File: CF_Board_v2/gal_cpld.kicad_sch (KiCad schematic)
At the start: 18 parts, among them J2 JTAG, U10 74LVC1G07, U16 74LVC1G08, U7 GAL, U8 CPLD, U9 74LVC1G08, X2 40MHz

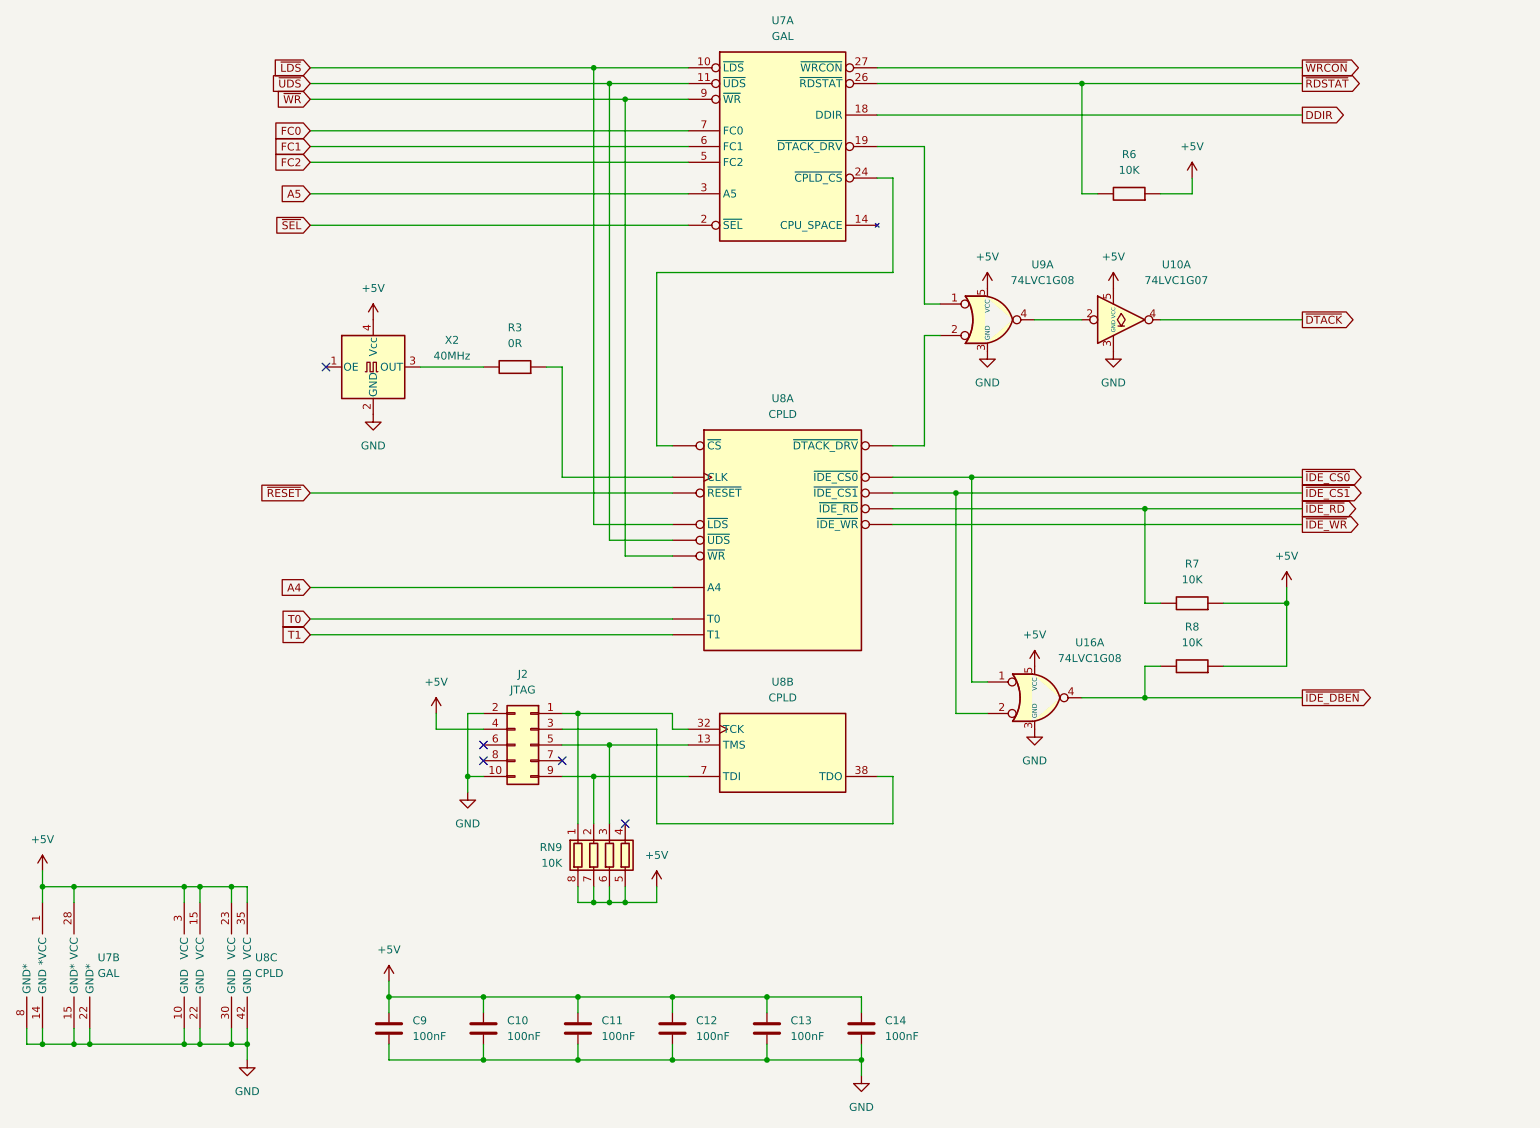
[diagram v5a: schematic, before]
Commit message: Modify control/status register to include CPLD timing select signals
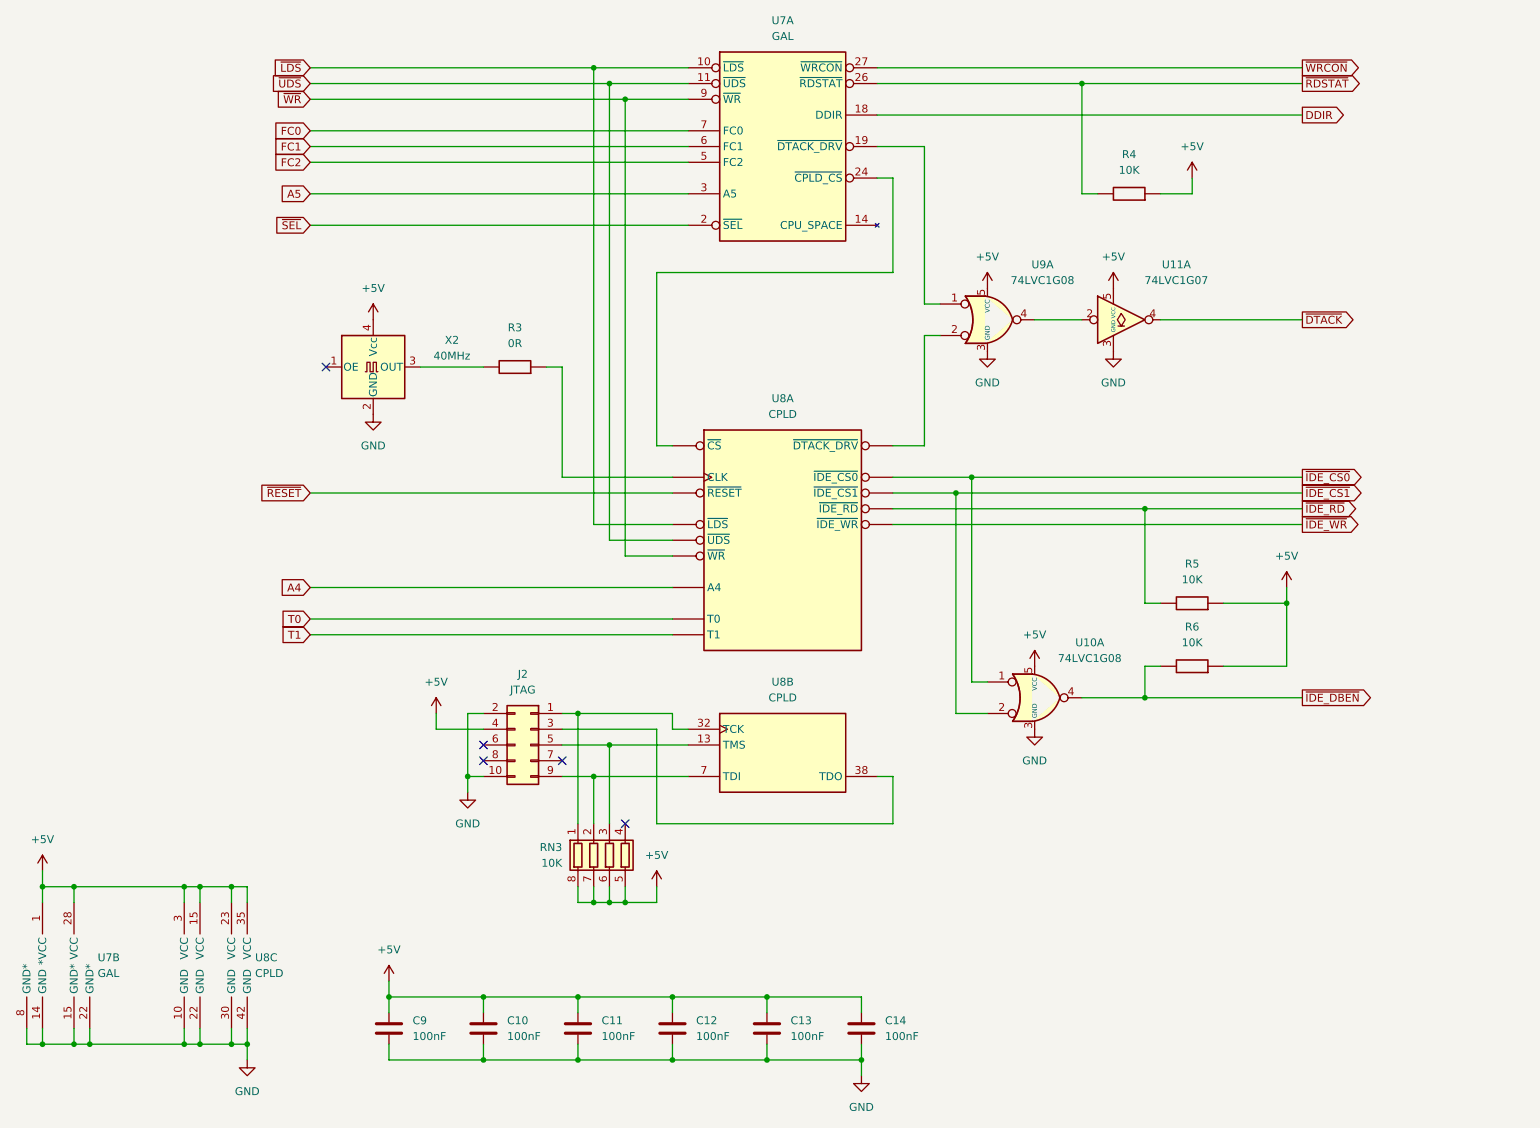
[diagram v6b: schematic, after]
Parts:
- renumbered R6 to R4, R7 to R5, R8 to R6, RN9 to RN3, U16 to U10, U10 to U11
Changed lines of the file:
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@@
   (symbol (lib_id "power:GND") (at 177.8 71.12 0) (unit 1)
     (in_bom yes) (on_board yes) (fields_autoplaced)
-    (property "Reference" "#PWR032" (id 0) (at 177.8 77.47 0)
+    (property "Reference" "#PWR035" (id 0) (at 177.8 77.47 0)
       (effects (font (size 1.27 1.27)) hide)
     )
@@
   (symbol (lib_id "power:+5V") (at 124.46 157.48 0) (unit 1)
     (in_bom yes) (on_board yes) (fields_autoplaced)
-    (property "Reference" "#PWR063" (id 0) (at 124.46 161.29 0)
+    (property "Reference" "#PWR032" (id 0) (at 124.46 161.29 0)
       (effects (font (size 1.27 1.27)) hide)
     )
@@
   (symbol (lib_id "COMET_symbols:74x1G08") (at 185.42 127 0) (unit 1) (convert 2)
     (in_bom yes) (on_board yes)
-    (property "Reference" "U16" (id 0) (at 194.31 118.11 0))
+    (property "Reference" "U10" (id 0) (at 194.31 118.11 0))
     (property "Value" "74LVC1G08" (id 1) (at 194.31 120.65 0))
     (property "Footprint" "COMET_footprints:Package_SOT23-5" (id 2) (at 185.42 127 0)
@@
   (symbol (lib_id "COMET_symbols:R") (at 200.66 45.72 90) (unit 1)
     (in_bom yes) (on_board yes) (fields_autoplaced)
-    (property "Reference" "R6" (id 0) (at 200.66 39.37 90))
+    (property "Reference" "R4" (id 0) (at 200.66 39.37 90))
     (property "Value" "10K" (id 1) (at 200.66 41.91 90))
     (property "Footprint" "COMET_footprints:R_SMD0805" (id 2) (at 200.66 45.72 0)
@@
   (symbol (lib_id "power:GND") (at 198.12 71.12 0) (unit 1)
     (in_bom yes) (on_board yes) (fields_autoplaced)
-    (property "Reference" "#PWR034" (id 0) (at 198.12 77.47 0)
+    (property "Reference" "#PWR039" (id 0) (at 198.12 77.47 0)
       (effects (font (size 1.27 1.27)) hide)
     )
@@
   (symbol (lib_id "power:+5V") (at 25.4 154.94 0) (unit 1)
     (in_bom yes) (on_board yes) (fields_autoplaced)
-    (property "Reference" "#PWR027" (id 0) (at 25.4 158.75 0)
+    (property "Reference" "#PWR025" (id 0) (at 25.4 158.75 0)
       (effects (font (size 1.27 1.27)) hide)
     )
@@
   (symbol (lib_id "power:+5V") (at 198.12 60.96 0) (unit 1)
     (in_bom yes) (on_board yes) (fields_autoplaced)
-    (property "Reference" "#PWR033" (id 0) (at 198.12 64.77 0)
+    (property "Reference" "#PWR038" (id 0) (at 198.12 64.77 0)
       (effects (font (size 1.27 1.27)) hide)
     )
@@
   (symbol (lib_id "COMET_symbols:74x1G08") (at 185.42 127 0) (unit 2)
     (in_bom yes) (on_board yes) (fields_autoplaced)
-    (property "Reference" "U16" (id 0) (at 186.69 125.7299 0)
+    (property "Reference" "U10" (id 0) (at 186.69 125.7299 0)
       (effects (font (size 1.27 1.27)) (justify left) hide)
     )
@@
   (symbol (lib_id "COMET_symbols:R") (at 210.82 121.92 90) (unit 1)
     (in_bom yes) (on_board yes) (fields_autoplaced)
-    (property "Reference" "R8" (id 0) (at 210.82 115.57 90))
+    (property "Reference" "R6" (id 0) (at 210.82 115.57 90))
     (property "Value" "10K" (id 1) (at 210.82 118.11 90))
     (property "Footprint" "COMET_footprints:R_SMD0805" (id 2) (at 210.82 121.92 0)
@@
   (symbol (lib_id "power:GND") (at 185.42 132.08 0) (unit 1)
     (in_bom yes) (on_board yes) (fields_autoplaced)
-    (property "Reference" "#PWR058" (id 0) (at 185.42 138.43 0)
+    (property "Reference" "#PWR037" (id 0) (at 185.42 138.43 0)
       (effects (font (size 1.27 1.27)) hide)
     )
@@
   (symbol (lib_id "power:+5V") (at 177.8 60.96 0) (unit 1)
     (in_bom yes) (on_board yes) (fields_autoplaced)
-    (property "Reference" "#PWR031" (id 0) (at 177.8 64.77 0)
+    (property "Reference" "#PWR034" (id 0) (at 177.8 64.77 0)
       (effects (font (size 1.27 1.27)) hide)
     )
@@
   (symbol (lib_id "power:GND") (at 58.42 185.42 0) (unit 1)
     (in_bom yes) (on_board yes) (fields_autoplaced)
-    (property "Reference" "#PWR028" (id 0) (at 58.42 191.77 0)
+    (property "Reference" "#PWR026" (id 0) (at 58.42 191.77 0)
       (effects (font (size 1.27 1.27)) hide)
     )
@@
   (symbol (lib_id "power:+5V") (at 226.06 109.22 0) (unit 1)
     (in_bom yes) (on_board yes) (fields_autoplaced)
-    (property "Reference" "#PWR059" (id 0) (at 226.06 113.03 0)
+    (property "Reference" "#PWR041" (id 0) (at 226.06 113.03 0)
       (effects (font (size 1.27 1.27)) hide)
     )
@@
   (symbol (lib_id "power:GND") (at 78.74 81.28 0) (unit 1)
     (in_bom yes) (on_board yes) (fields_autoplaced)
-    (property "Reference" "#PWR026" (id 0) (at 78.74 87.63 0)
+    (property "Reference" "#PWR028" (id 0) (at 78.74 87.63 0)
       (effects (font (size 1.27 1.27)) hide)
     )
@@
   (symbol (lib_id "power:GND") (at 157.48 187.96 0) (unit 1)
     (in_bom yes) (on_board yes) (fields_autoplaced)
-    (property "Reference" "#PWR030" (id 0) (at 157.48 194.31 0)
+    (property "Reference" "#PWR033" (id 0) (at 157.48 194.31 0)
       (effects (font (size 1.27 1.27)) hide)
     )
@@
   (symbol (lib_id "power:+5V") (at 88.9 129.54 0) (unit 1)
     (in_bom yes) (on_board yes) (fields_autoplaced)
-    (property "Reference" "#PWR061" (id 0) (at 88.9 133.35 0)
+    (property "Reference" "#PWR030" (id 0) (at 88.9 133.35 0)
       (effects (font (size 1.27 1.27)) hide)
     )
@@
   (symbol (lib_id "Device:R_Pack04") (at 116.84 152.4 0) (mirror x) (unit 1)
     (in_bom yes) (on_board yes) (fields_autoplaced)
-    (property "Reference" "RN9" (id 0) (at 109.22 151.1299 0)
+    (property "Reference" "RN3" (id 0) (at 109.22 151.1299 0)
       (effects (font (size 1.27 1.27)) (justify right))
     )
@@
   (symbol (lib_id "COMET_symbols:74x1G07") (at 198.12 66.04 0) (unit 2)
     (in_bom yes) (on_board yes) (fields_autoplaced)
-    (property "Reference" "U10" (id 0) (at 199.39 66.0399 0)
+    (property "Reference" "U11" (id 0) (at 199.39 66.0399 0)
       (effects (font (size 1.27 1.27)) (justify left) hide)
     )
@@
   (symbol (lib_id "COMET_symbols:74x1G07") (at 198.12 66.04 0) (unit 1) (convert 2)
     (in_bom yes) (on_board yes)
-    (property "Reference" "U10" (id 0) (at 208.28 57.15 0))
+    (property "Reference" "U11" (id 0) (at 208.28 57.15 0))
     (property "Value" "74LVC1G07" (id 1) (at 208.28 59.69 0))
     (property "Footprint" "COMET_footprints:Package_SOT23-5" (id 2) (at 198.12 66.04 0)
@@
   (symbol (lib_id "power:+5V") (at 185.42 121.92 0) (unit 1)
     (in_bom yes) (on_board yes) (fields_autoplaced)
-    (property "Reference" "#PWR057" (id 0) (at 185.42 125.73 0)
+    (property "Reference" "#PWR036" (id 0) (at 185.42 125.73 0)
       (effects (font (size 1.27 1.27)) hide)
     )
@@
   (symbol (lib_id "power:GND") (at 93.98 142.24 0) (unit 1)
     (in_bom yes) (on_board yes) (fields_autoplaced)
-    (property "Reference" "#PWR062" (id 0) (at 93.98 148.59 0)
+    (property "Reference" "#PWR031" (id 0) (at 93.98 148.59 0)
       (effects (font (size 1.27 1.27)) hide)
     )
@@
   (symbol (lib_id "COMET_symbols:R") (at 210.82 111.76 90) (unit 1)
     (in_bom yes) (on_board yes) (fields_autoplaced)
-    (property "Reference" "R7" (id 0) (at 210.82 105.41 90))
+    (property "Reference" "R5" (id 0) (at 210.82 105.41 90))
     (property "Value" "10K" (id 1) (at 210.82 107.95 90))
     (property "Footprint" "COMET_footprints:R_SMD0805" (id 2) (at 210.82 111.76 0)
@@
   (symbol (lib_id "power:+5V") (at 78.74 66.04 0) (unit 1)
     (in_bom yes) (on_board yes) (fields_autoplaced)
-    (property "Reference" "#PWR025" (id 0) (at 78.74 69.85 0)
+    (property "Reference" "#PWR027" (id 0) (at 78.74 69.85 0)
       (effects (font (size 1.27 1.27)) hide)
     )
@@
   (symbol (lib_id "power:+5V") (at 210.82 43.18 0) (unit 1)
     (in_bom yes) (on_board yes) (fields_autoplaced)
-    (property "Reference" "#PWR060" (id 0) (at 210.82 46.99 0)
-      (effects (font (size 1.27 1.27)) hide)
-    )
+    (property "Reference" "#PWR040" (id 0) (at 210.82 46.99 0)
+      (effects (font (size 1.27 1.27)) hide)
+    )
